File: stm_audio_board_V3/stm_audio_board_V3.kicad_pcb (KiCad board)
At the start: 4 copper layers, 66.1 x 75.8 mm, 149 parts, among them J1 Power conn, J2 STlink, J3 Audio_sig, J4 Conn_01x01_taptempo, J6 Conn_01x03_pot_ext, SW1 SW_SPST, U2 OP275, U3 MP-K7805-500R3, U4 OP275, U5 MIC2920A-3.3WS-TR, U6 L7809, U7 STM32H723ZGTx, U9 MIC2920A-3.3WS-TR, Y2 X1E0000210132

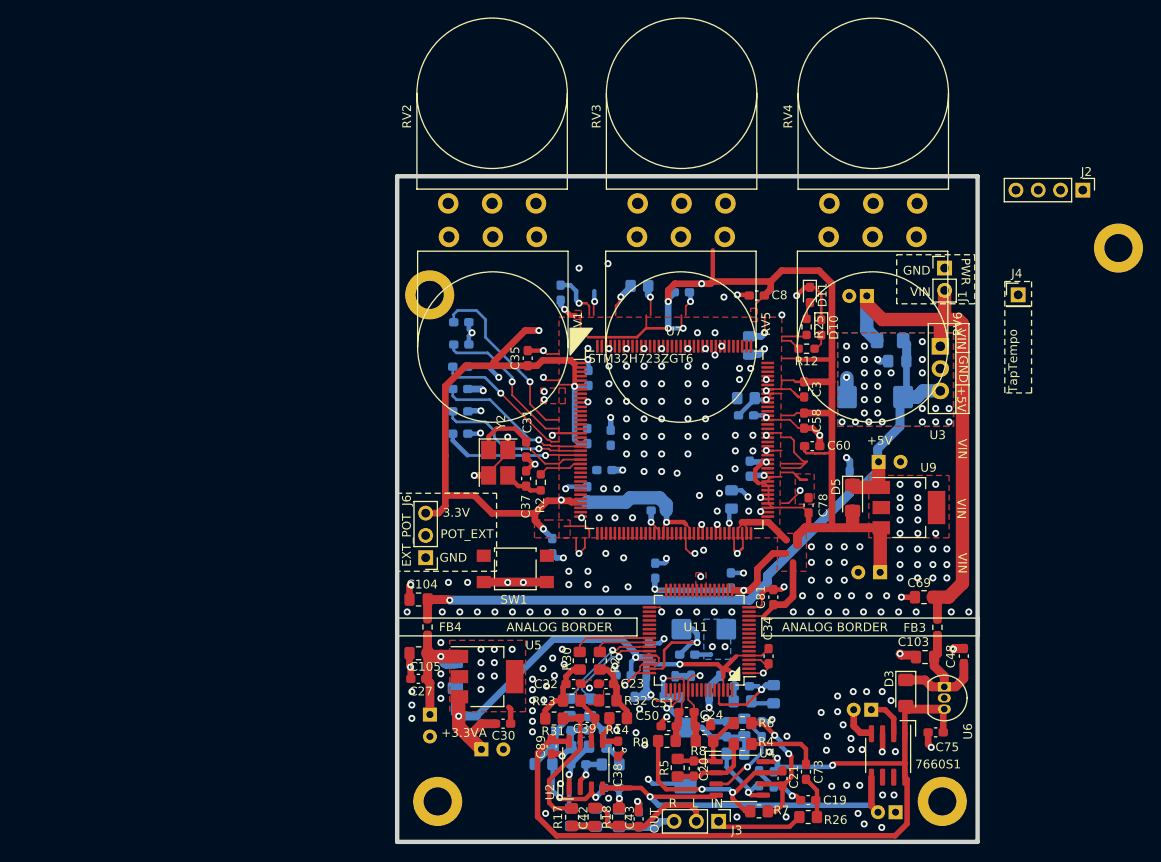
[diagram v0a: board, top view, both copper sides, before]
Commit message: SDRAM symbol added
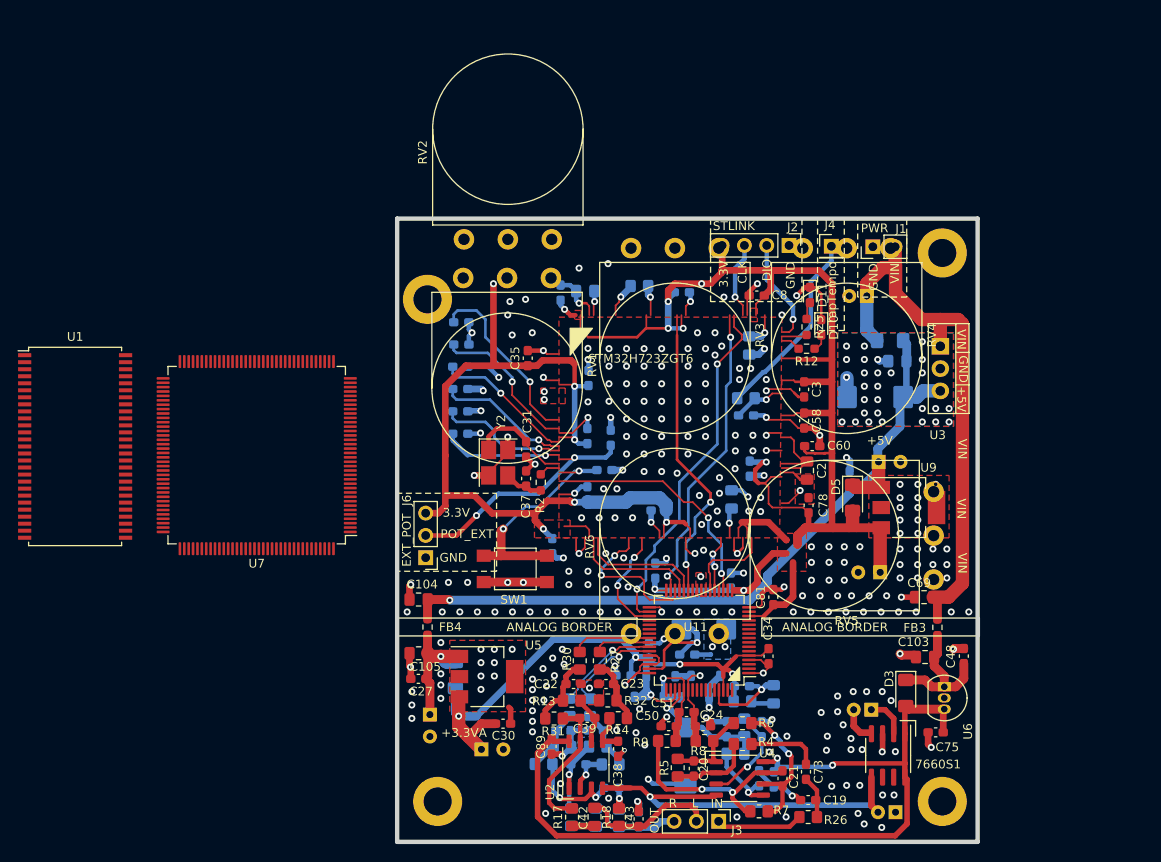
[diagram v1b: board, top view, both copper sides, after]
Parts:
- added C2: 2.2uF, Capacitor_SMD:C_0805_2012Metric_Pad1.18x1.45mm_HandSolder, F.Cu at (229.7, 74.6)
- added C52: 2.2uF, Capacitor_SMD:C_0805_2012Metric_Pad1.18x1.45mm_HandSolder, B.Cu at (204.4, 54.2)
- added U1: AS4C4M16SA, Package_SO:TSOP-II-54_22.2x10.16mm_P0.8mm, F.Cu at (146.3, 71.9)
- moved U7 47.6 mm to (167.0, 72.9), turned to 180 degrees
- moved RV6 46.9 mm to (219.6, 93.2), turned to 90 degrees
- moved RV5 44.6 mm to (244.1, 77.0), turned to 180 degrees
- moved J2 34.1 mm to (227.6, 49.0)
- moved J4 22.0 mm to (232.5, 49.1)
- moved H3 20.1 mm to (245.1, 49.8)
- moved RV4 14.0 mm to (229.2, 49.3), turned to -90 degrees
- moved RV3 11.9 mm to (209.6, 49.3), turned to -90 degrees
- moved J1 8.53 mm to (237.2, 49.1), turned to 90 degrees
- moved RV1 4.96 mm to (190.5, 52.7)
- moved RV2 4.47 mm to (200.6, 48.3)
- moved H4 0.57 mm to (186.4, 55.1)
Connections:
- C1 pad 1: Net-(C1-Pad1) -> unconnected-(C1-Pad1)
- C49 pad 1: Net-(C49-Pad1) -> unconnected-(C49-Pad1)
- R1 pad 1: Net-(U7-BOOT0) -> unconnected-(R1-Pad1)
- U7 pad 106: Net-(C49-Pad1) -> unconnected-(U7-VCAP-Pad106)
- U7 pad 107: GND -> Net-(U7-VSS-Pad107)
- U7 pad 108: +3.3V -> unconnected-(U7-VDD-Pad108)
- U7 pad 111: AD1939_I2S2_CK -> unconnected-(U7-PC10-Pad111)
- U7 pad 120: GND -> Net-(U7-VSS-Pad107)
- U7 pad 121: +3.3V -> unconnected-(U7-VDD-Pad121)
- U7 pad 13: POT1 -> unconnected-(U7-PF3-Pad13)
- U7 pad 130: GND -> Net-(U7-VSS-Pad107)
- U7 pad 131: +3.3V -> unconnected-(U7-VDD-Pad131)
- U7 pad 138: Net-(U7-BOOT0) -> unconnected-(U7-BOOT0-Pad138)
- U7 pad 143: GND -> unconnected-(U7-PDR_ON-Pad143)
- U7 pad 144: +3.3V -> unconnected-(U7-VDD-Pad144)
- U7 pad 15: POT2 -> unconnected-(U7-PF5-Pad15)
- U7 pad 16: GND -> Net-(U7-VSS-Pad107)
- U7 pad 17: +3.3V -> unconnected-(U7-VDD-Pad17)
- U7 pad 19: POT3 -> unconnected-(U7-PF7-Pad19)
- U7 pad 20: POT4 -> unconnected-(U7-PF8-Pad20)
- U7 pad 21: POT5 -> unconnected-(U7-PF9-Pad21)
- U7 pad 22: POT6 -> unconnected-(U7-PF10-Pad22)
- U7 pad 23: OSC0 -> unconnected-(U7-PH0-Pad23)
- U7 pad 24: OSC1 -> unconnected-(U7-PH1-Pad24)
- U7 pad 25: /MCU/NRST -> unconnected-(U7-NRST-Pad25)
- U7 pad 28: AD1939_I2S1_SDI -> unconnected-(U7-PC2_C-Pad28)
- U7 pad 30: +3.3V -> unconnected-(U7-VDD-Pad30)
- U7 pad 31: GND -> unconnected-(U7-VSSA-Pad31)
- U7 pad 32: +3.3V -> unconnected-(U7-VREF+-Pad32)
- U7 pad 33: +3.3V -> unconnected-(U7-VDDA-Pad33)
- U7 pad 38: GND -> Net-(U7-VSS-Pad107)
- U7 pad 39: +3.3V -> unconnected-(U7-VDD-Pad39)
- U7 pad 40: AD1939_I2S2_WS -> unconnected-(U7-PA4-Pad40)
- U7 pad 41: AD1939_SPI3_CLK -> unconnected-(U7-PA5-Pad41)
- U7 pad 42: AD1939_SPI3_MISO -> unconnected-(U7-PA6-Pad42)
- U7 pad 43: AD1939_SPI3_MOSI -> unconnected-(U7-PA7-Pad43)
- U7 pad 48: AD1939_I2S2_SDO -> unconnected-(U7-PB2-Pad48)
- U7 pad 51: GND -> Net-(U7-VSS-Pad107)
- U7 pad 52: +3.3V -> unconnected-(U7-VDD-Pad52)
- U7 pad 6: +3.3V -> unconnected-(U7-VBAT-Pad6)
- U7 pad 61: GND -> Net-(U7-VSS-Pad107)
- U7 pad 62: +3.3V -> unconnected-(U7-VDD-Pad62)
- U7 pad 69: AD1939_I2S1_CK -> unconnected-(U7-PB10-Pad69)
- U7 pad 71: Net-(C1-Pad1) -> unconnected-(U7-VCAP-Pad71)
- U7 pad 72: +3.3V -> unconnected-(U7-VDD-Pad72)
- U7 pad 73: AD1939_I2S1_WS -> unconnected-(U7-PB12-Pad73)
- U7 pad 83: GND -> Net-(U7-VSS-Pad107)
- U7 pad 84: +3.3V -> unconnected-(U7-VDD-Pad84)
- U7 pad 94: GND -> Net-(U7-VSS-Pad107)
- U7 pad 95: +3.3V -> unconnected-(U7-VDD33USB-Pad95)
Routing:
- net AD1939_SPI3_CLK: track 0.00 -> 40.3 mm, vias 0 -> 2
- net AD1939_SPI3_MISO: track 0.00 -> 34.6 mm, vias 0 -> 2
- net AD1939_I2S1_SDI: track 0.00 -> 34.2 mm, vias 0 -> 2
- net AD1939_I2S2_SDO: track 0.00 -> 27.7 mm, vias 0 -> 2
- net POT_EXT: track 0.00 -> 27.7 mm, vias 0 -> 2
- net /MCU/NRST: track 0.00 -> 26.0 mm, vias 0 -> 2
- net TAP_TEMPO_INPUT: track 0.00 -> 21.9 mm
- net AD1939_SPI3_MOSI: track 0.00 -> 17.4 mm, vias 0 -> 2
- net AD1939_I2S1_WS: track 0.00 -> 14.4 mm
- net AD1939_I2S1_CK: track 0.00 -> 14.4 mm
- net (no net): track 17.8 -> 3.92 mm, vias 1 -> 0
- net AD1939_SPI_CS: track 0.00 -> 12.5 mm, vias 0 -> 2
- net SWDIO: track 0.00 -> 12.2 mm, vias 0 -> 1
- net GND: track 187.2 -> 198.4 mm, vias 305 -> 312
- net /MCU/VDD_DSI: track 0.00 -> 11.0 mm
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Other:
- board size 66.1 x 75.8 mm -> 66.1 x 71 mm
- board text added: "CLK"
- board text added: "DIO"
- board text added: "STLINK"

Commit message: pcb redesign
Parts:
- removed C2, C52: 2.2uF, Capacitor_SMD:C_0805_2012Metric_Pad1.18x1.45mm_HandSolder
- U1: value AS4C4M16SA -> IS42S16100H-7TL; footprint Package_SO:TSOP-II-54_22.2x10.16mm_P0.8mm -> Library:TSOP-2-50-new
- moved RV6 76.9 mm to (220.4, 16.3)
- moved RV5 60.9 mm to (240.9, 16.2), turned to 90 degrees
- moved U7 47.3 mm to (214.1, 69.8), turned to 0 degrees
- moved C54 38.9 mm to (183.4, 29.6)
- moved C57 38.9 mm to (183.5, 22.0)
- moved C55 38.9 mm to (183.5, 19.4)
- moved C56 38.9 mm to (183.4, 32.1)
- moved C59 38.9 mm to (183.4, 24.5)
- moved C62 38.9 mm to (183.4, 27.0)
- moved RV1 31.6 mm to (190.7, 21.1)
- moved RV2 31.6 mm to (200.8, 16.7)
- moved RV3 28.2 mm to (210.3, 21.1)
- moved RV4 28.1 mm to (231.2, 21.3)
- moved C12 23.7 mm to (178.1, 57.7)
- moved H4 20.2 mm to (166.8, 50.3)
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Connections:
- C1 pad 1: unconnected-(C1-Pad1) -> Net-(C1-Pad1)
- C49 pad 1: unconnected-(C49-Pad1) -> Net-(C49-Pad1)
- R1 pad 1: unconnected-(R1-Pad1) -> Net-(U7-BOOT0)
- U1 pad 1: Net-(U1-VDD-Pad1) -> unconnected-(U1B-VDD-Pad1)
- U1 pad 12: Net-(U1-VSSQ-Pad12) -> unconnected-(U1A-DQ7-Pad12)
- U1 pad 14: Net-(U1-VDD-Pad1) -> unconnected-(U1A-LDQM-Pad14)
- U1 pad 27: Net-(U1-VDD-Pad1) -> unconnected-(U1A-A4-Pad27)
- U1 pad 28: Net-(U1-VSS-Pad28) -> unconnected-(U1A-A5-Pad28)
- U1 pad 3: Net-(U1-VDDQ-Pad3) -> unconnected-(U1A-DQ1-Pad3)
- U1 pad 41: Net-(U1-VSS-Pad28) -> unconnected-(U1B-GNDQ-Pad41)
- U1 pad 43: Net-(U1-VDDQ-Pad3) -> unconnected-(U1A-DQ11-Pad43)
- U1 pad 46: Net-(U1-VSSQ-Pad12) -> unconnected-(U1A-DQ13-Pad46)
- U1 pad 49: Net-(U1-VDDQ-Pad3) -> unconnected-(U1A-DQ15-Pad49)
- U1 pad 6: Net-(U1-VSSQ-Pad12) -> unconnected-(U1A-DQ3-Pad6)
- U1 pad 9: Net-(U1-VDDQ-Pad3) -> unconnected-(U1A-DQ5-Pad9)
- U7 pad 106: unconnected-(U7-VCAP-Pad106) -> Net-(C49-Pad1)
- U7 pad 107: Net-(U7-VSS-Pad107) -> GND
- U7 pad 108: unconnected-(U7-VDD-Pad108) -> +3.3V
- U7 pad 111: unconnected-(U7-PC10-Pad111) -> AD1939_I2S2_CK
- U7 pad 120: Net-(U7-VSS-Pad107) -> GND
- U7 pad 121: unconnected-(U7-VDD-Pad121) -> +3.3V
- U7 pad 13: unconnected-(U7-PF3-Pad13) -> POT1
- U7 pad 130: Net-(U7-VSS-Pad107) -> GND
- U7 pad 131: unconnected-(U7-VDD-Pad131) -> +3.3V
- U7 pad 138: unconnected-(U7-BOOT0-Pad138) -> Net-(U7-BOOT0)
- U7 pad 143: unconnected-(U7-PDR_ON-Pad143) -> GND
- U7 pad 144: unconnected-(U7-VDD-Pad144) -> +3.3V
- U7 pad 15: unconnected-(U7-PF5-Pad15) -> POT2
- U7 pad 16: Net-(U7-VSS-Pad107) -> GND
- U7 pad 17: unconnected-(U7-VDD-Pad17) -> +3.3V
- U7 pad 19: unconnected-(U7-PF7-Pad19) -> POT3
- U7 pad 20: unconnected-(U7-PF8-Pad20) -> POT4
- U7 pad 21: unconnected-(U7-PF9-Pad21) -> POT5
- U7 pad 22: unconnected-(U7-PF10-Pad22) -> POT6
- U7 pad 23: unconnected-(U7-PH0-Pad23) -> OSC0
- U7 pad 24: unconnected-(U7-PH1-Pad24) -> OSC1
- U7 pad 25: unconnected-(U7-NRST-Pad25) -> /MCU/NRST
- U7 pad 28: unconnected-(U7-PC2_C-Pad28) -> AD1939_I2S1_SDI
- U7 pad 30: unconnected-(U7-VDD-Pad30) -> +3.3V
- U7 pad 31: unconnected-(U7-VSSA-Pad31) -> GND
- U7 pad 32: unconnected-(U7-VREF+-Pad32) -> +3.3V
- U7 pad 33: unconnected-(U7-VDDA-Pad33) -> +3.3V
- U7 pad 38: Net-(U7-VSS-Pad107) -> GND
- U7 pad 39: unconnected-(U7-VDD-Pad39) -> +3.3V
- U7 pad 40: unconnected-(U7-PA4-Pad40) -> AD1939_I2S2_WS
- U7 pad 41: unconnected-(U7-PA5-Pad41) -> AD1939_SPI3_CLK
- U7 pad 42: unconnected-(U7-PA6-Pad42) -> AD1939_SPI3_MISO
- U7 pad 43: unconnected-(U7-PA7-Pad43) -> AD1939_SPI3_MOSI
- U7 pad 48: unconnected-(U7-PB2-Pad48) -> AD1939_I2S2_SDO
- U7 pad 51: Net-(U7-VSS-Pad107) -> GND
- U7 pad 52: unconnected-(U7-VDD-Pad52) -> +3.3V
- U7 pad 6: unconnected-(U7-VBAT-Pad6) -> +3.3V
- U7 pad 61: Net-(U7-VSS-Pad107) -> GND
- U7 pad 62: unconnected-(U7-VDD-Pad62) -> +3.3V
- U7 pad 69: unconnected-(U7-PB10-Pad69) -> AD1939_I2S1_CK
- U7 pad 71: unconnected-(U7-VCAP-Pad71) -> Net-(C1-Pad1)
- U7 pad 72: unconnected-(U7-VDD-Pad72) -> +3.3V
- U7 pad 73: unconnected-(U7-PB12-Pad73) -> AD1939_I2S1_WS
- U7 pad 83: Net-(U7-VSS-Pad107) -> GND
- U7 pad 84: unconnected-(U7-VDD-Pad84) -> +3.3V
- U7 pad 94: Net-(U7-VSS-Pad107) -> GND
- U7 pad 95: unconnected-(U7-VDD33USB-Pad95) -> +3.3V
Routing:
- net +3.3V: track 302.5 -> 39.2 mm, vias 14 -> 2
- net GND: track 198.4 -> 108.4 mm, vias 312 -> 196
- net AD1939_SPI3_CLK: track 40.3 -> 0.00 mm, vias 2 -> 0
- net AD1939_SPI3_MISO: track 34.6 -> 0.00 mm, vias 2 -> 0
- net AD1939_I2S1_SDI: track 34.2 -> 0.00 mm, vias 2 -> 0
- net AD1939_I2S2_SDO: track 27.7 -> 0.00 mm, vias 2 -> 0
- net POT_EXT: track 27.7 -> 0.00 mm, vias 2 -> 0
- net /MCU/NRST: track 26.0 -> 0.00 mm, vias 2 -> 0
- net TAP_TEMPO_INPUT: track 21.9 -> 0.00 mm
- net POT1: track 20.9 -> 0.00 mm, vias 1 -> 0
- net POT2: track 17.5 -> 0.00 mm, vias 1 -> 0
- net POT3: track 16.1 -> 0.00 mm, vias 1 -> 0
- net POT4: track 15.3 -> 0.00 mm, vias 1 -> 0
- net POT5: track 14.9 -> 0.00 mm, vias 1 -> 0
- net AD1939_I2S1_WS: track 14.4 -> 0.00 mm
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
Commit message: Input and output stages are made and assembly started on pcb view
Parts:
- removed D2, D3, D5: 1N4148, Diode_SMD:D_1206_3216Metric_Pad1.42x1.75mm_HandSolder
- removed RV1, RV2, RV3, RV4, RV5, RV6: R_Potentiometer, Potentiometer_THT:Potentiometer_Omeg_PC16BU_Vertical
- added C100: 120p, Capacitor_SMD:C_0603_1608Metric, F.Cu at (111.7, 59.4)
- added C101: 1nF, Capacitor_SMD:C_0603_1608Metric, F.Cu at (105.8, 66.5)
- added C106: 1nF, Capacitor_SMD:C_0603_1608Metric, F.Cu at (108.8, 66.5)
- added C107: 100pF, Capacitor_SMD:C_0603_1608Metric, F.Cu at (107.3, 68.1)
- added C108: 560p, Capacitor_SMD:C_0603_1608Metric, F.Cu at (125.7, 97.2)
- added C109: 560p, Capacitor_SMD:C_0603_1608Metric, F.Cu at (125.7, 99.7)
- added C110: 68p, Capacitor_SMD:C_0603_1608Metric, F.Cu at (125.7, 102.2)
- added C111: 68p, Capacitor_SMD:C_0603_1608Metric, F.Cu at (125.7, 104.7)
- added C112: 2u2, Capacitor_SMD:C_0805_2012Metric_Pad1.18x1.45mm_HandSolder, F.Cu at (138.7, 115.1)
- added C113: 2.2nF, Capacitor_SMD:C_0603_1608Metric, F.Cu at (125.7, 107.2)
- added C114: 560p, Capacitor_SMD:C_0603_1608Metric, F.Cu at (125.7, 109.7)
- added C115: 560p, Capacitor_SMD:C_0603_1608Metric, F.Cu at (125.7, 112.2)
- added C116: 68p, Capacitor_SMD:C_0603_1608Metric, F.Cu at (125.7, 114.7)
- added C117: 68p, Capacitor_SMD:C_0603_1608Metric, F.Cu at (125.7, 117.2)
- added C118: 2u2, Capacitor_SMD:C_0805_2012Metric_Pad1.18x1.45mm_HandSolder, F.Cu at (138.7, 118.1)
- added C119: 2.2nF, Capacitor_SMD:C_0603_1608Metric, F.Cu at (125.7, 119.7)
- added C2: 10p, Capacitor_SMD:C_0603_1608Metric, F.Cu at (198.6, 60.2)
- added C52: 100n, Capacitor_SMD:C_0603_1608Metric, F.Cu at (198.7, 58.6)
- added C53: 100n, Capacitor_SMD:C_0603_1608Metric, F.Cu at (201.6, 60.3)
- added C65: 10p, Capacitor_SMD:C_0603_1608Metric, F.Cu at (202.4, 57.7)
- added C66: 100n, Capacitor_SMD:C_0603_1608Metric, F.Cu at (213.1, 62.6)
- added C72: 120p, Capacitor_SMD:C_0603_1608Metric, F.Cu at (211.4, 59.2)
- added C74: 1nF, Capacitor_SMD:C_0603_1608Metric, F.Cu at (205.5, 66.4)
- added C82: 1nF, Capacitor_SMD:C_0603_1608Metric, F.Cu at (208.5, 66.4)
- added C83: 100pF, Capacitor_SMD:C_0603_1608Metric, F.Cu at (207.3, 67.9)
- added C84: 10p, Capacitor_SMD:C_0603_1608Metric, F.Cu at (148.1, 60.0)
- added C85: 100n, Capacitor_SMD:C_0603_1608Metric, F.Cu at (148.1, 58.5)
- added C86: 100n, Capacitor_SMD:C_0603_1608Metric, F.Cu at (151.1, 60.0)
- added C87: 10p, Capacitor_SMD:C_0603_1608Metric, F.Cu at (151.9, 57.7)
- added C88: 100n, Capacitor_SMD:C_0603_1608Metric, F.Cu at (162.6, 62.1)
- added C91: 120p, Capacitor_SMD:C_0603_1608Metric, F.Cu at (161.0, 58.9)
- added C92: 1nF, Capacitor_SMD:C_0603_1608Metric, F.Cu at (155.1, 66.0)
- added C93: 1nF, Capacitor_SMD:C_0603_1608Metric, F.Cu at (158.1, 66.0)
- added C94: 100pF, Capacitor_SMD:C_0603_1608Metric, F.Cu at (156.7, 67.6)
- added C95: 10p, Capacitor_SMD:C_0603_1608Metric, F.Cu at (98.6, 60.5)
- added C96: 100n, Capacitor_SMD:C_0603_1608Metric, F.Cu at (98.6, 58.9)
- added C97: 100n, Capacitor_SMD:C_0603_1608Metric, F.Cu at (101.7, 60.5)
- added C98: 10p, Capacitor_SMD:C_0603_1608Metric, F.Cu at (102.5, 58.1)
- added C99: 100n, Capacitor_SMD:C_0603_1608Metric, F.Cu at (113.3, 62.5)
- added J10: USB_A, Connector_USB:USB_A_CONNFLY_DS1095-WNR0, F.Cu at (264.1, 142.2)
- added J11: AudioJack_Loop1_Return, Connector_Audio:Jack_6.35mm_Neutrik_NMJ6HCD2_Horizontal, F.Cu at (197.4, 46.4)
- added J12: AudioJack_Loop1_Send, Connector_Audio:Jack_6.35mm_Neutrik_NMJ6HCD2_Horizontal, F.Cu at (222.4, 46.7)
- added J13: AudioJack_INPUT_Main, Connector_Audio:Jack_6.35mm_Neutrik_NMJ6HCD2_Horizontal, F.Cu at (247.4, 46.7)
- added J14: AudioJack_OUTPUT_Main, Connector_Audio:Jack_6.35mm_Neutrik_NMJ6HCD2_Horizontal, F.Cu at (73.1, 46.1)
- added J15: AudioJack_Loop2_Send, Connector_Audio:Jack_6.35mm_Neutrik_NMJ6HCD2_Horizontal, F.Cu at (172.9, 46.1)
- added J5: Barrel_Jack_MountingPin, Connector_BarrelJack:BarrelJack_CUI_PJ-063AH_Horizontal, F.Cu at (260.1, 114.5)
- added J7: AudioJack_Loop3_Return, Connector_Audio:Jack_6.35mm_Neutrik_NMJ6HCD2_Horizontal, F.Cu at (97.4, 46.7)
- added J8: AudioJack_Loop3_Send, Connector_Audio:Jack_6.35mm_Neutrik_NMJ6HCD2_Horizontal, F.Cu at (122.4, 46.7)
- added J9: AudioJack_Loop2_Return, Connector_Audio:Jack_6.35mm_Neutrik_NMJ6HCD2_Horizontal, F.Cu at (147.4, 46.7)
- added R28: 100R, Resistor_SMD:R_0603_1608Metric, F.Cu at (198.6, 61.8)
- added R29: 1M, Resistor_SMD:R_0603_1608Metric, F.Cu at (198.6, 57.1)
- added R34: 100R, Resistor_SMD:R_0603_1608Metric, F.Cu at (201.6, 61.8)
- added R35: 1M, Resistor_SMD:R_0603_1608Metric, F.Cu at (201.0, 57.7)
- added R36: 5.76k, Resistor_SMD:R_0603_1608Metric, F.Cu at (206.6, 55.9)
- added R37: 100R, Resistor_SMD:R_0603_1608Metric, F.Cu at (211.5, 62.6)
- added R38: 5.76k, Resistor_SMD:R_0603_1608Metric, F.Cu at (213.0, 59.2)
- added R39: 240R, Resistor_SMD:R_0603_1608Metric, F.Cu at (206.3, 64.1)
- added R40: 240R, Resistor_SMD:R_0603_1608Metric, F.Cu at (207.8, 64.1)
- added R41: 100R, Resistor_SMD:R_0603_1608Metric, F.Cu at (148.1, 61.6)
- added R42: 1M, Resistor_SMD:R_0603_1608Metric, F.Cu at (148.1, 57.0)
- added R43: 100R, Resistor_SMD:R_0603_1608Metric, F.Cu at (151.2, 61.6)
- added R44: 1M, Resistor_SMD:R_0603_1608Metric, F.Cu at (150.4, 57.7)
- added R45: 5.76k, Resistor_SMD:R_0603_1608Metric, F.Cu at (155.9, 55.4)
- added R46: 100R, Resistor_SMD:R_0603_1608Metric, F.Cu at (161.0, 62.1)
- added R47: 5.76k, Resistor_SMD:R_0603_1608Metric, F.Cu at (162.5, 58.9)
- added R48: 240R, Resistor_SMD:R_0603_1608Metric, F.Cu at (155.8, 63.7)
- added R49: 240R, Resistor_SMD:R_0603_1608Metric, F.Cu at (157.3, 63.7)
- added R50: 100R, Resistor_SMD:R_0603_1608Metric, F.Cu at (98.6, 62.1)
- added R51: 1M, Resistor_SMD:R_0603_1608Metric, F.Cu at (98.6, 57.3)
- added R52: 100R, Resistor_SMD:R_0603_1608Metric, F.Cu at (101.7, 62.1)
- added R53: 1M, Resistor_SMD:R_0603_1608Metric, F.Cu at (100.9, 58.1)
- added R54: 5.76k, Resistor_SMD:R_0603_1608Metric, F.Cu at (106.4, 55.9)
- added R55: 100R, Resistor_SMD:R_0603_1608Metric, F.Cu at (111.7, 62.6)
- added R56: 5.76k, Resistor_SMD:R_0603_1608Metric, F.Cu at (113.3, 59.4)
- added R57: 240R, Resistor_SMD:R_0603_1608Metric, F.Cu at (106.6, 64.3)
- added R58: 240R, Resistor_SMD:R_0603_1608Metric, F.Cu at (108.1, 64.3)
- added R59: 3k, Resistor_SMD:R_0603_1608Metric, F.Cu at (138.7, 97.4)
- added R60: 3k, Resistor_SMD:R_0603_1608Metric, F.Cu at (138.7, 100.3)
- added R61: 3k, Resistor_SMD:R_0603_1608Metric, F.Cu at (138.7, 103.3)
- added R62: 3k, Resistor_SMD:R_0603_1608Metric, F.Cu at (138.7, 106.2)
- added R63: 3k, Resistor_SMD:R_0603_1608Metric, F.Cu at (138.7, 109.2)
- added R64: 3k, Resistor_SMD:R_0603_1608Metric, F.Cu at (138.7, 112.1)
- added R65: 604, Resistor_SMD:R_0603_1608Metric, F.Cu at (143.4, 97.4)
- added R66: 10k, Resistor_SMD:R_0603_1608Metric, F.Cu at (143.4, 100.3)
- added R67: 3k, Resistor_SMD:R_0603_1608Metric, F.Cu at (143.4, 103.3)
- added R68: 3k, Resistor_SMD:R_0603_1608Metric, F.Cu at (143.4, 106.2)
- added R69: 3k, Resistor_SMD:R_0603_1608Metric, F.Cu at (143.4, 109.2)
- added R70: 3k, Resistor_SMD:R_0603_1608Metric, F.Cu at (143.4, 112.1)
- added R71: 3k, Resistor_SMD:R_0603_1608Metric, F.Cu at (148.2, 97.4)
- added R72: 3k, Resistor_SMD:R_0603_1608Metric, F.Cu at (148.2, 100.3)
- added R73: 604, Resistor_SMD:R_0603_1608Metric, F.Cu at (148.2, 103.3)
- added R74: 10k, Resistor_SMD:R_0603_1608Metric, F.Cu at (148.2, 106.2)
- added U10: OP275, Package_SO:SSOP-8_3.9x5.05mm_P1.27mm, F.Cu at (156.5, 59.1)
- added U12: OP275, Package_SO:SSOP-8_3.9x5.05mm_P1.27mm, F.Cu at (107.2, 59.6)
- added U14: OP275, Package_SO:SSOP-8_3.9x5.05mm_P1.27mm, F.Cu at (132.1, 105.8)
- added U8: OP275, Package_SO:SSOP-8_3.9x5.05mm_P1.27mm, F.Cu at (206.9, 59.6)
- C1, C13, C15, C26, C28, C29, C4, C46, C49, C67, C70, C71, C76, C77, C80, D1, D4, D6, D8, D9, R33: moved to F.Cu
- C10, C102, C11, C12, C14, C16, C25, C32, C33, C36, C5, C54, C55, C56, C57, C59, C6, C61, C62, C63, C64, C7, C79, C9, C90: value 100nF -> 100n; footprint Capacitor_SMD:C_0603_1608Metric_Pad1.08x0.95mm_HandSolder -> Capacitor_SMD:C_0603_1608Metric; moved to F.Cu
- C17, C18: value 68n -> 100n; footprint Capacitor_SMD:C_0603_1608Metric_Pad1.08x0.95mm_HandSolder -> Capacitor_SMD:C_0603_1608Metric; moved to F.Cu
- C19, C20, C21, C23, C24, C38, C39, C43, C50, C51: footprint Capacitor_SMD:C_0603_1608Metric_Pad1.08x0.95mm_HandSolder -> Capacitor_SMD:C_0603_1608Metric
- C22: value 270p -> 560p; footprint Capacitor_SMD:C_0603_1608Metric_Pad1.08x0.95mm_HandSolder -> Capacitor_SMD:C_0603_1608Metric
- C27, C3, C30, C34, C35, C48, C58, C60, C75, C78, C8, C81, C89: value 100nF -> 100n; footprint Capacitor_SMD:C_0603_1608Metric_Pad1.08x0.95mm_HandSolder -> Capacitor_SMD:C_0603_1608Metric
- C31, C37: value 9pF -> 10p; footprint Capacitor_SMD:C_0603_1608Metric_Pad1.08x0.95mm_HandSolder -> Capacitor_SMD:C_0603_1608Metric
- C40: value 270p -> 560p; footprint Capacitor_SMD:C_0603_1608Metric_Pad1.08x0.95mm_HandSolder -> Capacitor_SMD:C_0603_1608Metric; moved to F.Cu
- C41, C44, C45, C47, C68: footprint Capacitor_SMD:C_0603_1608Metric_Pad1.08x0.95mm_HandSolder -> Capacitor_SMD:C_0603_1608Metric; moved to F.Cu
- C73: value 68n -> 100n; footprint Capacitor_SMD:C_0603_1608Metric_Pad1.08x0.95mm_HandSolder -> Capacitor_SMD:C_0603_1608Metric
- R1, R10, R11, R21, R23, R24, R3: footprint Resistor_SMD:R_0805_2012Metric_Pad1.20x1.40mm_HandSolder -> Resistor_SMD:R_0603_1608Metric; moved to F.Cu
- R12: value 1k NC -> 1k
- R13, R17, R18, R5, R6, R7, R8, R9: footprint Resistor_SMD:R_0805_2012Metric_Pad1.20x1.40mm_HandSolder -> Resistor_SMD:R_0603_1608Metric
- R14: value 1.5k -> 3k; footprint Resistor_SMD:R_0805_2012Metric_Pad1.20x1.40mm_HandSolder -> Resistor_SMD:R_0603_1608Metric
- R15, R19: value 11k -> 3k; footprint Resistor_SMD:R_0805_2012Metric_Pad1.20x1.40mm_HandSolder -> Resistor_SMD:R_0603_1608Metric; moved to F.Cu
- R16, R20: value 5.6k -> 3k; footprint Resistor_SMD:R_0805_2012Metric_Pad1.20x1.40mm_HandSolder -> Resistor_SMD:R_0603_1608Metric; moved to F.Cu
- R2: value 100R NC -> 100R; footprint Resistor_SMD:R_0603_1608Metric_Pad0.98x0.95mm_HandSolder -> Resistor_SMD:R_0603_1608Metric
- R22: value 1.5k -> 3k; footprint Resistor_SMD:R_0805_2012Metric_Pad1.20x1.40mm_HandSolder -> Resistor_SMD:R_0603_1608Metric; moved to F.Cu
- R26: value 100 -> 100R; footprint Resistor_SMD:R_0805_2012Metric_Pad1.20x1.40mm_HandSolder -> Resistor_SMD:R_0603_1608Metric
- R27, R32: value 5.6k -> 3k; footprint Resistor_SMD:R_0805_2012Metric_Pad1.20x1.40mm_HandSolder -> Resistor_SMD:R_0603_1608Metric
- R30, R31: value 11k -> 3k; footprint Resistor_SMD:R_0805_2012Metric_Pad1.20x1.40mm_HandSolder -> Resistor_SMD:R_0603_1608Metric
- R4: value 500k -> 1M; footprint Resistor_SMD:R_0805_2012Metric_Pad1.20x1.40mm_HandSolder -> Resistor_SMD:R_0603_1608Metric
- moved H3 182.6 mm to (82.1, 113.4)
- moved D11 172.1 mm to (84.2, 146.1), turned to 0 degrees
- moved R25 169.9 mm to (80.7, 139.9), turned to 0 degrees
- moved R12 167.5 mm to (80.7, 137.4), turned to 0 degrees
- moved H2 163.1 mm to (82.1, 106.2)
- moved D10 162.8 mm to (89.9, 138.9), turned to 0 degrees
- moved J1 159.1 mm to (92.6, 97.8)
- moved C49 157.6 mm to (85.3, 136.7), turned to 0 degrees
- moved J4 150.6 mm to (92.6, 105.0)
- moved R1 149.3 mm to (85.2, 139.6)
- moved J2 148.0 mm to (88.0, 97.8), turned to 0 degrees
- moved C1 146.8 mm to (85.3, 133.7), turned to 0 degrees
- moved C8 144.2 mm to (99.1, 126.9), turned to 0 degrees
- moved C63 142.6 mm to (99.1, 139.4), turned to 0 degrees
- moved R33 142.0 mm to (99.3, 136.7), turned to 0 degrees
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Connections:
- C38 pad 2: Net-(U2B-+) -> Net-(U2A-+)
- C39 pad 1: Net-(U2B--) -> Net-(U2A--)
- C42 pad 2: GUITAR_OUT_L/MONO -> Audio_Main_Output
- C43 pad 2: GUITAR_OUT_L/MONO -> Audio_Main_Output
- C44 pad 1: Net-(U2A--) -> Net-(U2B--)
- C45 pad 2: Net-(U2A-+) -> Net-(U2B-+)
- C46 pad 2: GUITAR_OUT_R -> Audio_Loop1_Send
- C47 pad 2: GUITAR_OUT_R -> Audio_Loop1_Send
- R13 pad 2: Net-(U2B--) -> Net-(U2A--)
- R14 pad 1: Net-(U2B-+) -> Net-(U2A-+)
- R15 pad 1: DAC2N -> DAC1P
- R16 pad 1: DAC2P -> DAC1N
- R18 pad 1: GUITAR_OUT_L/MONO -> Audio_Main_Output
- R21 pad 1: Net-(U2A--) -> Net-(C40-Pad2)
- R21 pad 2: Net-(C40-Pad2) -> Net-(U2B--)
- R22 pad 1: Net-(U2A-+) -> Net-(U2B-+)
- R24 pad 1: GUITAR_OUT_R -> Audio_Loop1_Send
- R26 pad 1: GUITAR_IN -> Audio_Main_Input
- U2 pad 1: Net-(C44-Pad2) -> Net-(C39-Pad2)
- U2 pad 7: Net-(C39-Pad2) -> Net-(C44-Pad2)
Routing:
- net GND: track 108.4 -> 1.61 mm, vias 196 -> 1
- net +9V: track 94.5 -> 0.00 mm, vias 2 -> 0
- net 5V: track 86.9 -> 0.00 mm, vias 1 -> 0
- net +3.3VA: track 80.2 -> 0.00 mm, vias 5 -> 0
- net ADC1N: track 11.5 -> 78.3 mm, vias 1 -> 2
- net ADC1P: track 14.7 -> 79.6 mm, vias 1 -> 2
- net PWR_INPUT_12V-18V: track 55.9 -> 0.00 mm
- net -9V: track 44.5 -> 0.00 mm, vias 1 -> 0
- net +3.3V: track 39.2 -> 0.00 mm, vias 2 -> 0
- net Audio_Loop1_Send: track 0.00 -> 28.5 mm
- net DAC1N: track 6.49 -> 25.9 mm
- net AD1939_SPI3_MOSI: track 17.4 -> 0.00 mm, vias 2 -> 0
- net Net-(C39-Pad2): track 16.2 -> 0.00 mm
- net GUITAR_OUT_L/MONO: track 15.6 -> 0.00 mm
- net Net-(U6-IN): track 15.5 -> 0.00 mm
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- removed copper zone on F.Cu, net +3.3V
- removed copper zone on B.Cu, net GND
- removed copper zone on F.Cu, net GND
- removed copper zone on In1.Cu, net GND
- removed copper zone on In2.Cu, net GND
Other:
- board size 66.1 x 71 mm -> 201 x 117 mm
- board text added: "1M"
- board text added: "C50"
- board text added: "INPUT_MAIN"
- board text added: "LOOP1_RETURN"
- board text added: "LOOP1_SEND"
- board text added: "LOOP2_RETURN"
- board text added: "LOOP2_SEND"
- board text added: "LOOP3_RETURN"
- board text added: "LOOP3_SEND"
- board text added: "OUTPUT_MAIN"
- board text added: "R5"
- board text added: "R9"
- board text removed: "+3.3VA"
- board text removed: "Auth: Papp Aron"
- board text removed: "Date: 2024.02.09."
- board text removed: "JLCJLCJLCJLC"
- board text removed: "STM32H747IGT6"
- board text removed: "STM_AUDIO_BOARD_V3"
- board text removed: "WARNING! VIN: 12-18V min 500mA"
